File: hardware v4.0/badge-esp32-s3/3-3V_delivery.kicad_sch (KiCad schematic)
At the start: 24 parts, among them Q4 HL2301A, Q7 AO3424, U2 TPS630701RNMR, U8 TLV75733PDBVR

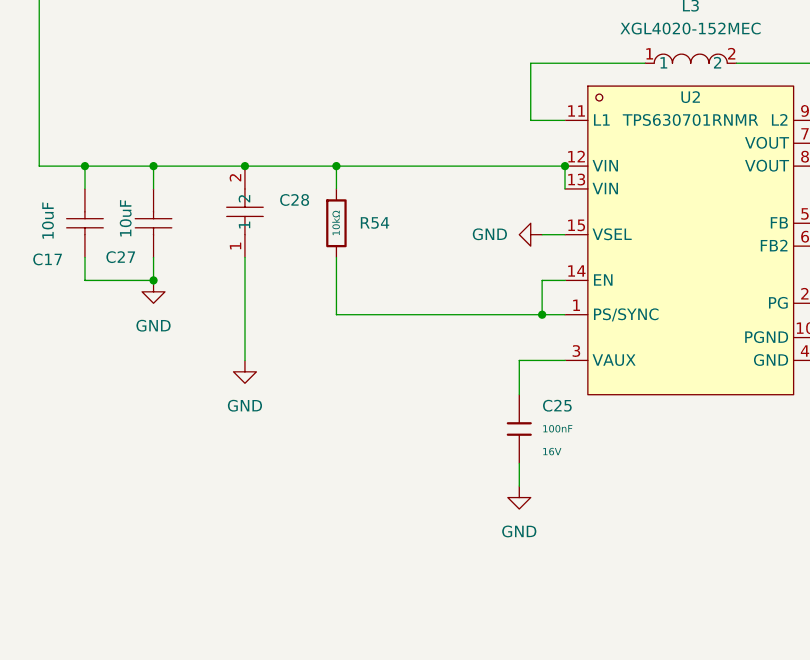
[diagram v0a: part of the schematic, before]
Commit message: started changes for 4.0.1
fixed footprint, joystick collision, Changed to Forced PWM mode for boost converter, Fixed some silkscreen errors
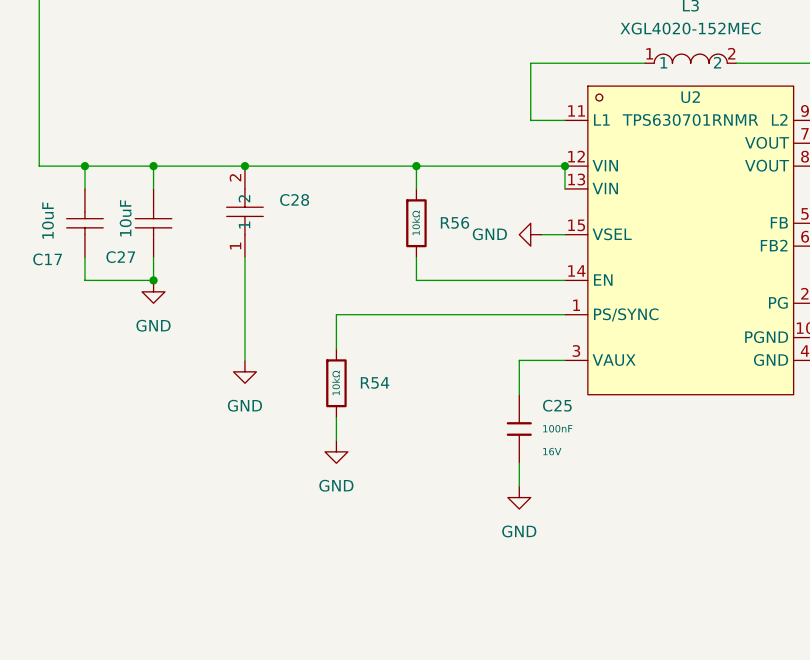
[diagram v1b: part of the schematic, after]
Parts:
- added R56: 10kΩ, PCM_JLCPCB:R_0402, symbol PCM_JLCPCB-Resistors:0402,10kΩ
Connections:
- net GND: now also R54.2
- net VCC_5V: now also R56.1; no longer R54.1
- new net: R54.1, U2.1 (PS/SYNC)
- new net: R56.2, U2.14 (EN)
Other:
- moved on the sheet: R54
